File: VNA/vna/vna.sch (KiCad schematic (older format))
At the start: 4 parts, among them J1 USB_B_Micro, J2 Battery Cell Connection, J3 Pt1, J4 Pt2

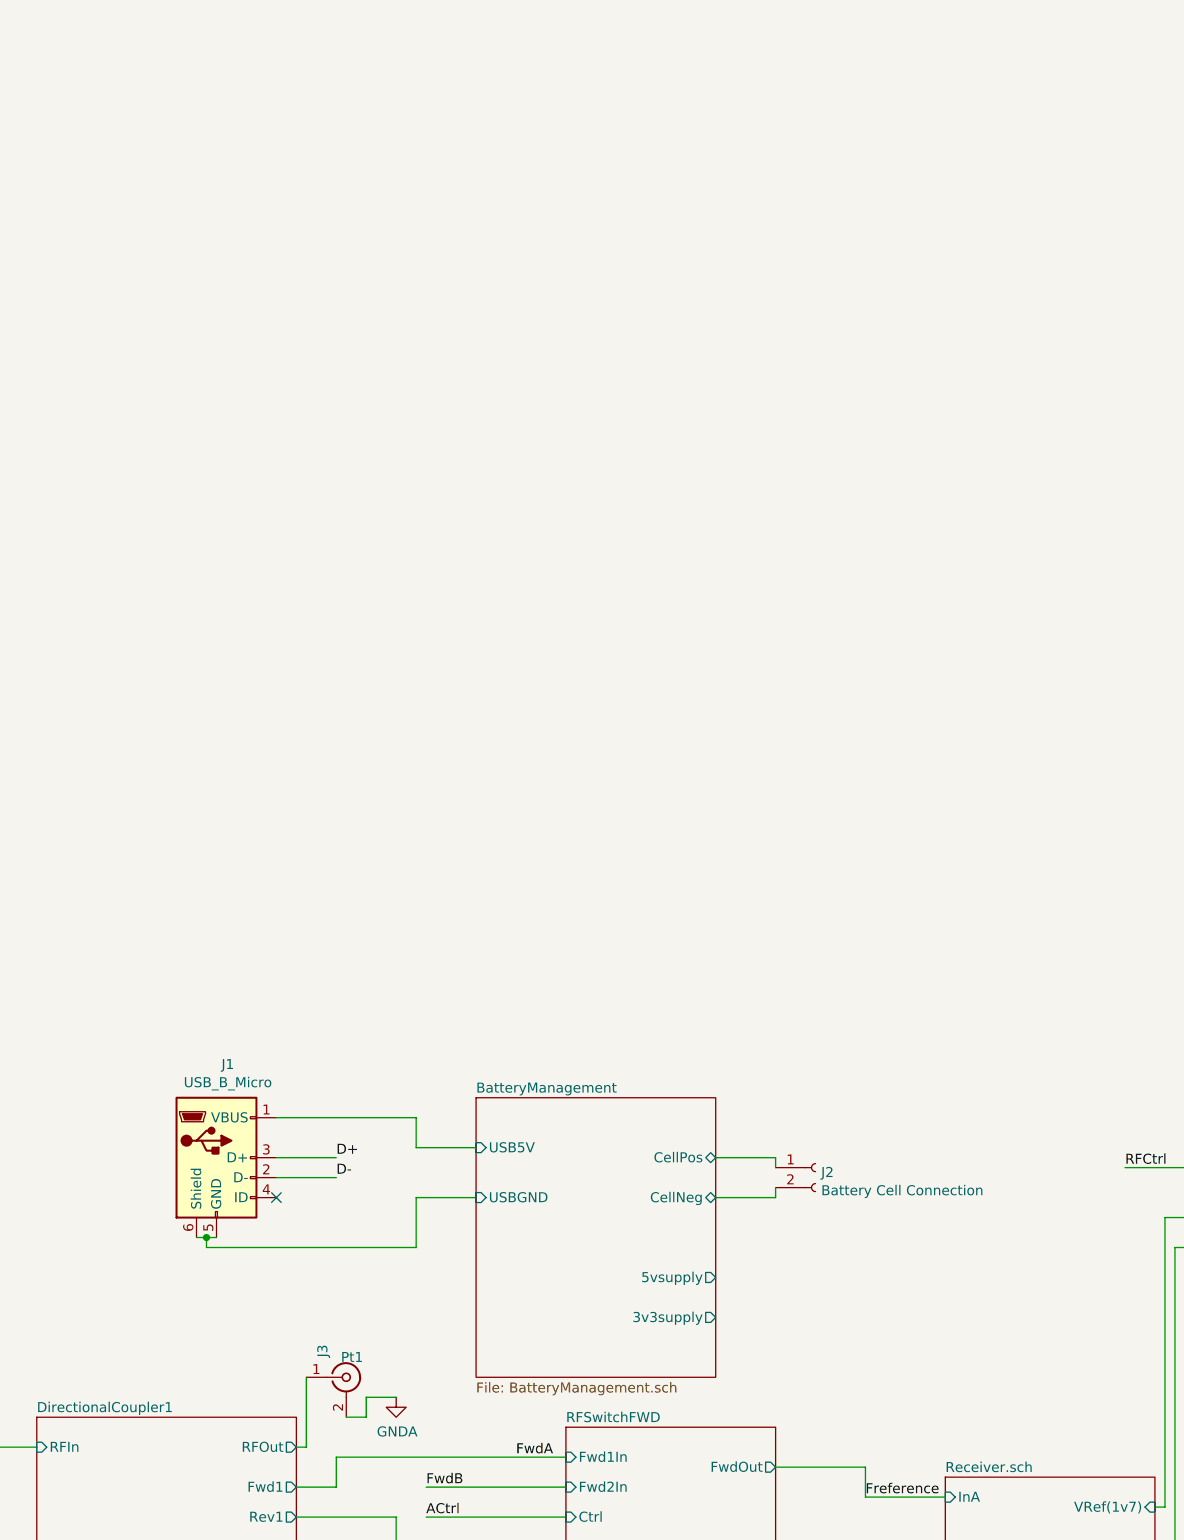
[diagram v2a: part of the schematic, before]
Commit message: changed inductors to a single transformer component
inductors in the directional couplers was changed to a single transformer

this will help with later layout opperations
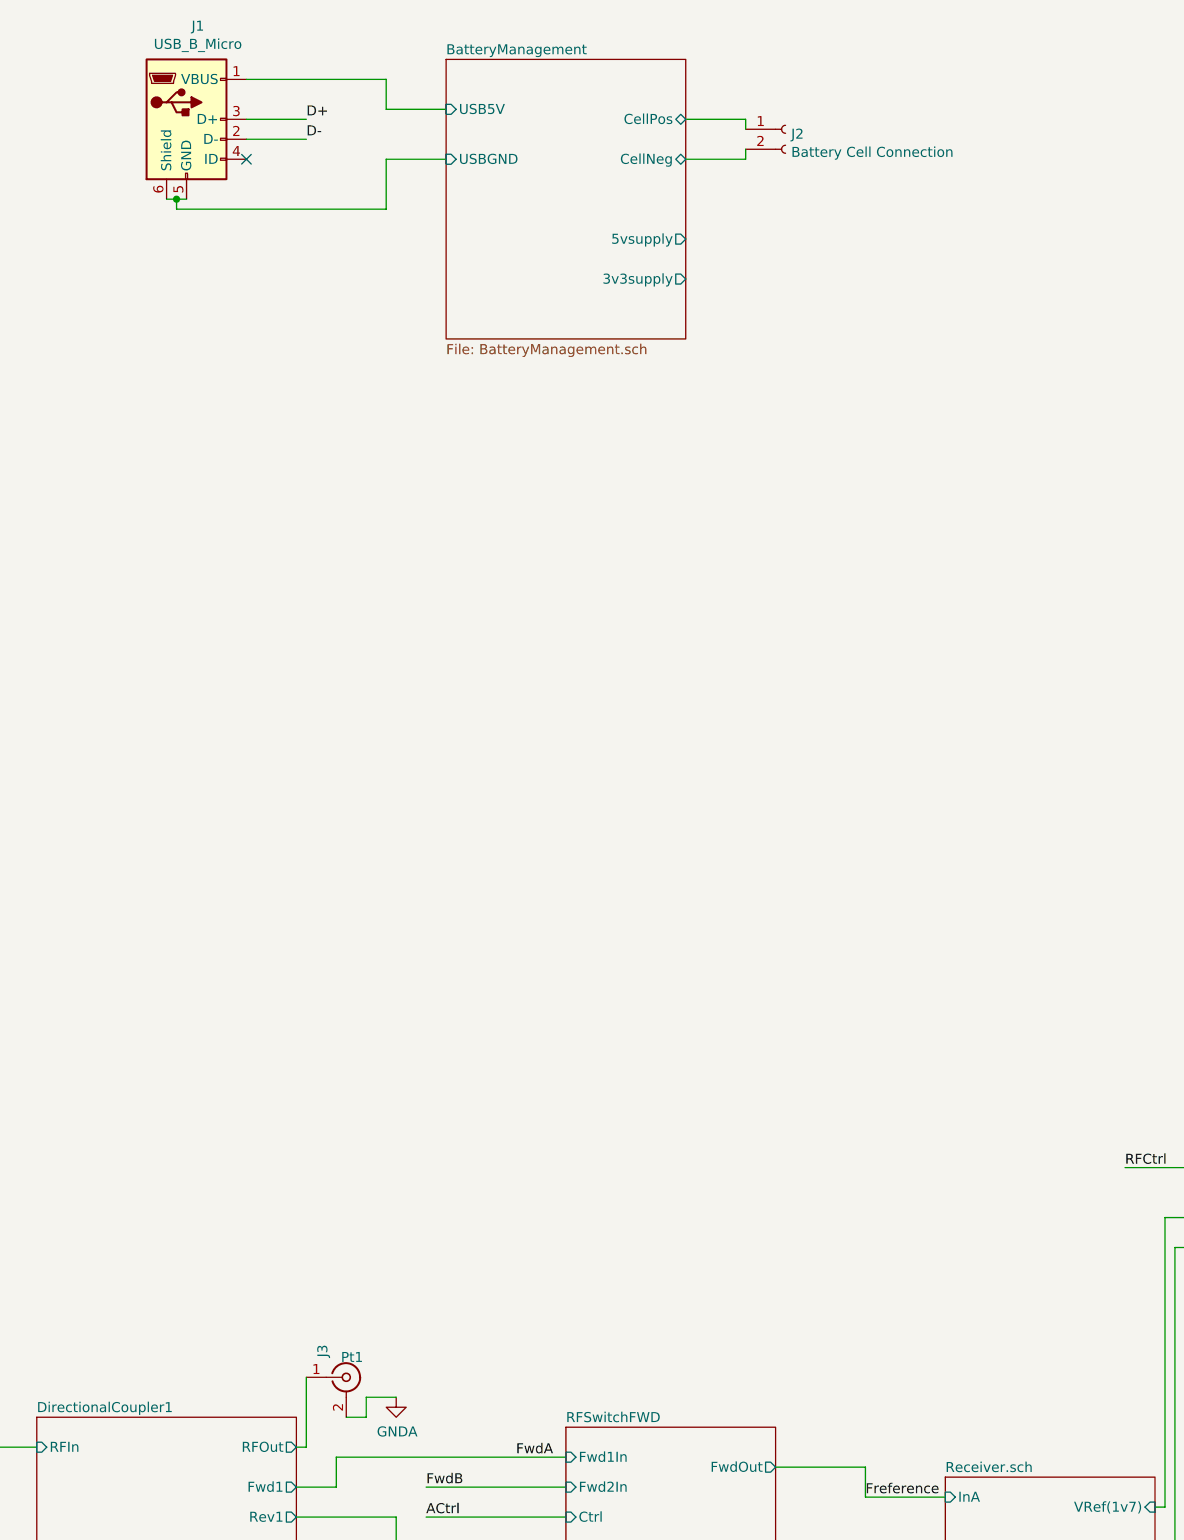
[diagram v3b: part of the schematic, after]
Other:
- moved on the sheet: J1, J2
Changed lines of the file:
@@
 BCtrl
 $Sheet
-S 5500 2250 1200 1400
+S 5350 -2950 1200 1400
 U 5CDF1C56
 F0 "BatteryManagement" 50
 F1 "BatteryManagement.sch" 50
-F2 "USB5V" I L 5500 2500 50
-F3 "USBGND" I L 5500 2750 50
-F4 "3v3supply" O R 6700 3350 50
-F5 "5vsupply" O R 6700 3150 50
-F6 "CellPos" B R 6700 2550 50
-F7 "CellNeg" B R 6700 2750 50
+F2 "USB5V" I L 5350 -2700 50
+F3 "USBGND" I L 5350 -2450 50
+F4 "3v3supply" O R 6550 -1850 50
+F5 "5vsupply" O R 6550 -2050 50
+F6 "CellPos" B R 6550 -2650 50
+F7 "CellNeg" B R 6550 -2450 50
 $EndSheet
 $Comp
 L Connector:USB_B_Micro J1
 U 1 1 5CE2753D
-P 4200 2550
-F 0 "J1" H 4257 3017 50  0000 C CNN
-F 1 "USB_B_Micro" H 4257 2926 50  0000 C CNN
-F 2 "" H 4350 2500 50  0001 C CNN
-F 3 "~" H 4350 2500 50  0001 C CNN
-	1    4200 2550
+P 4050 -2650
+F 0 "J1" H 4107 -2183 50  0000 C CNN
+F 1 "USB_B_Micro" H 4107 -2274 50  0000 C CNN
+F 2 "" H 4200 -2700 50  0001 C CNN
+F 3 "~" H 4200 -2700 50  0001 C CNN
+	1    4050 -2650
 	1    0    0    -1
 $EndComp
 Wire Wire Line
-	4500 2350 5200 2350
+	4350 -2850 5050 -2850
 Wire Wire Line
-	5200 2350 5200 2500
+	5050 -2850 5050 -2700
 Wire Wire Line
-	5200 2500 5500 2500
+	5050 -2700 5350 -2700
 Wire Wire Line
-	4100 2950 4150 2950
+	3950 -2250 4000 -2250
 Wire Wire Line
-	4150 2950 4150 3000
+	4000 -2250 4000 -2200
 Wire Wire Line
-	4150 3000 5200 3000
+	4000 -2200 5050 -2200
 Wire Wire Line
-	5200 3000 5200 2750
+	5050 -2200 5050 -2450
 Wire Wire Line
-	5200 2750 5500 2750
-Connection ~ 4150 2950
+	5050 -2450 5350 -2450
+Connection ~ 4000 -2250
 Wire Wire Line
-	4150 2950 4200 2950
+	4000 -2250 4050 -2250
 $Sheet
 S 9250 2300 900  950
@@
 Text Label 10700 2700 0    50   ~ 0
 D+
-NoConn ~ 4500 2750
+NoConn ~ 4350 -2450
 Wire Wire Line
-	4500 2550 4800 2550
+	4350 -2650 4650 -2650
 Wire Wire Line
-	4500 2650 4800 2650
-Text Label 4800 2550 0    50   ~ 0
+	4350 -2550 4650 -2550
+Text Label 4650 -2650 0    50   ~ 0
 D+
-Text Label 4800 2650 0    50   ~ 0
+Text Label 4650 -2550 0    50   ~ 0
 D-
 Wire Wire Line
@@
 L Connector:Conn_01x02_Female J2
 U 1 1 5CE4F062
-P 7200 2600
-F 0 "J2" H 7228 2576 50  0000 L CNN
-F 1 "Battery Cell Connection" H 7228 2485 50  0000 L CNN
-F 2 "" H 7200 2600 50  0001 C CNN
-F 3 "~" H 7200 2600 50  0001 C CNN
-	1    7200 2600
+P 7050 -2600
+F 0 "J2" H 7078 -2624 50  0000 L CNN
+F 1 "Battery Cell Connection" H 7078 -2715 50  0000 L CNN
+F 2 "" H 7050 -2600 50  0001 C CNN
+F 3 "~" H 7050 -2600 50  0001 C CNN
+	1    7050 -2600
 	1    0    0    -1
 $EndComp
 Wire Wire Line
-	6700 2550 7000 2550
+	6550 -2650 6850 -2650
 Wire Wire Line
-	7000 2550 7000 2600
+	6850 -2650 6850 -2600
 Wire Wire Line
-	6700 2750 7000 2750
+	6550 -2450 6850 -2450
 Wire Wire Line
-	7000 2750 7000 2700
+	6850 -2450 6850 -2500
 Wire Wire Line
 	1450 4350 1200 4350

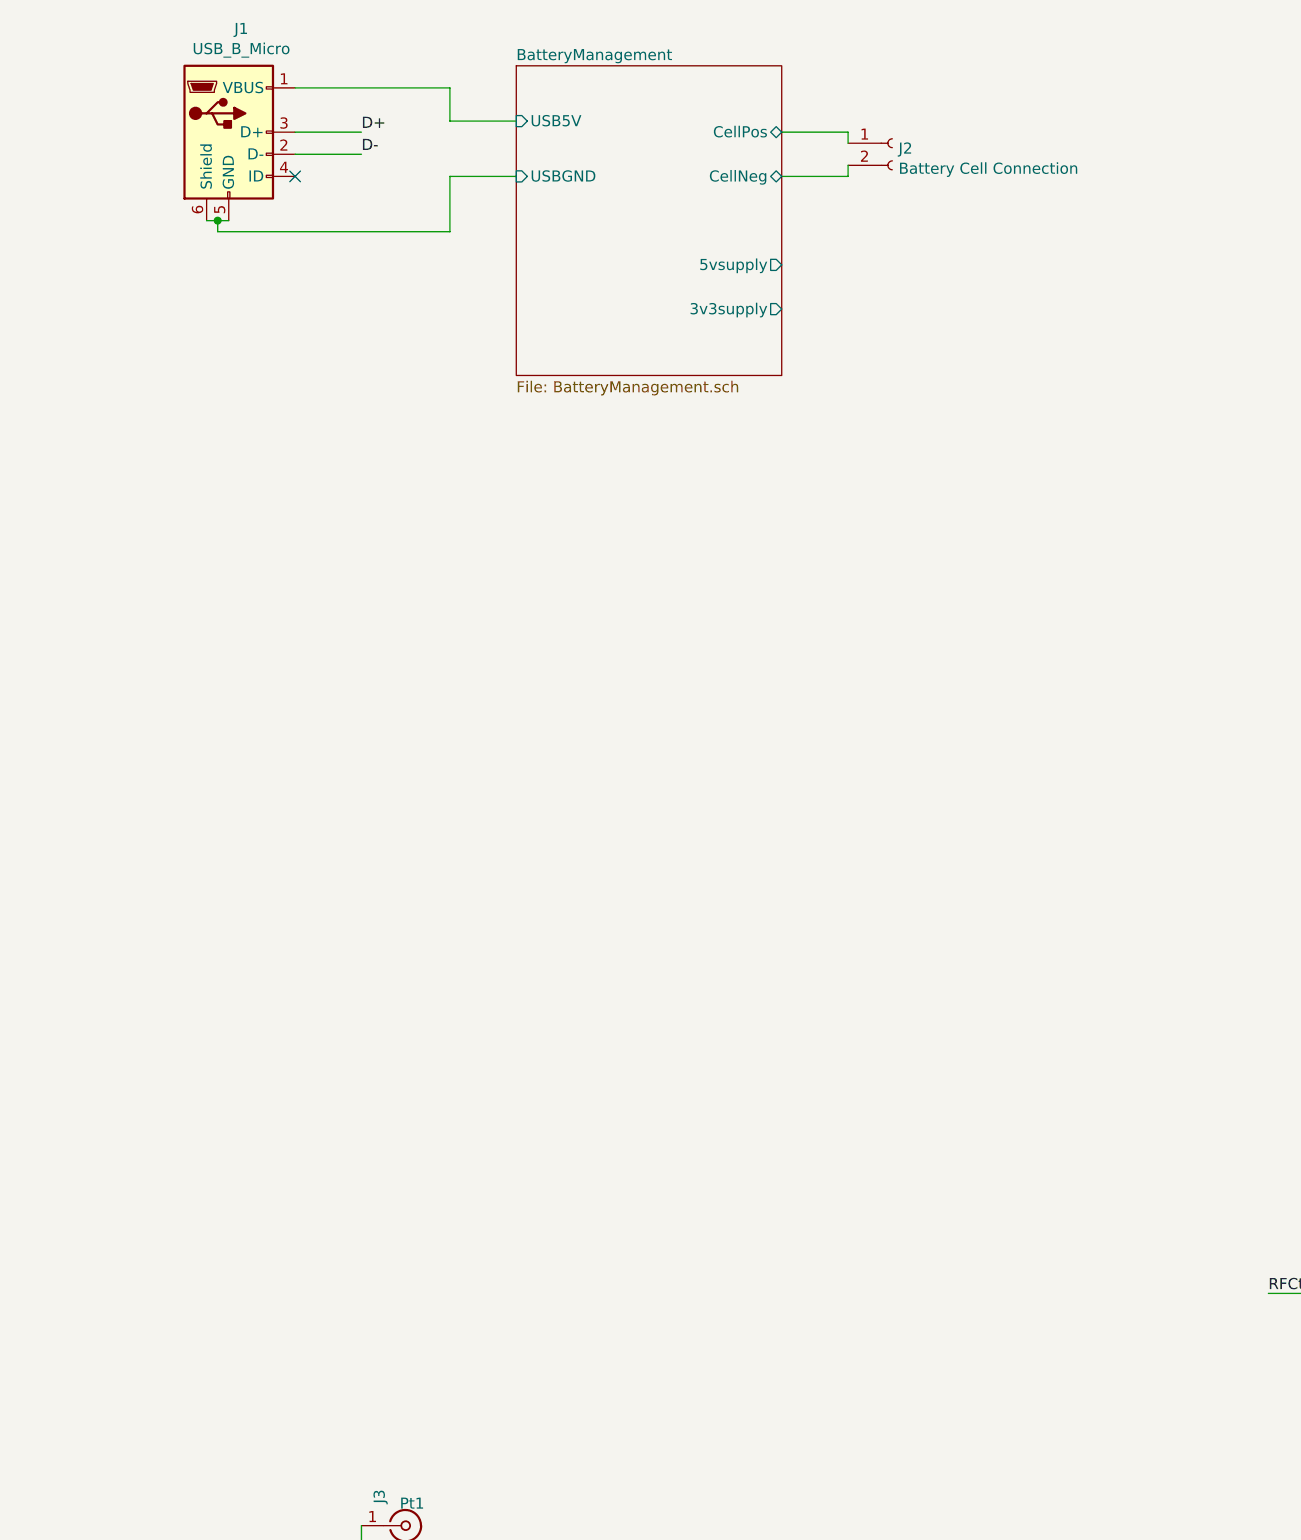
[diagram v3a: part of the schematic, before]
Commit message: micro-controller pins labelled
micro controller pins have been labelled, the pins on the bottom are yet to be linked to them.

still to wire up ftdi chip,

still to decide upon rf switch control schema.
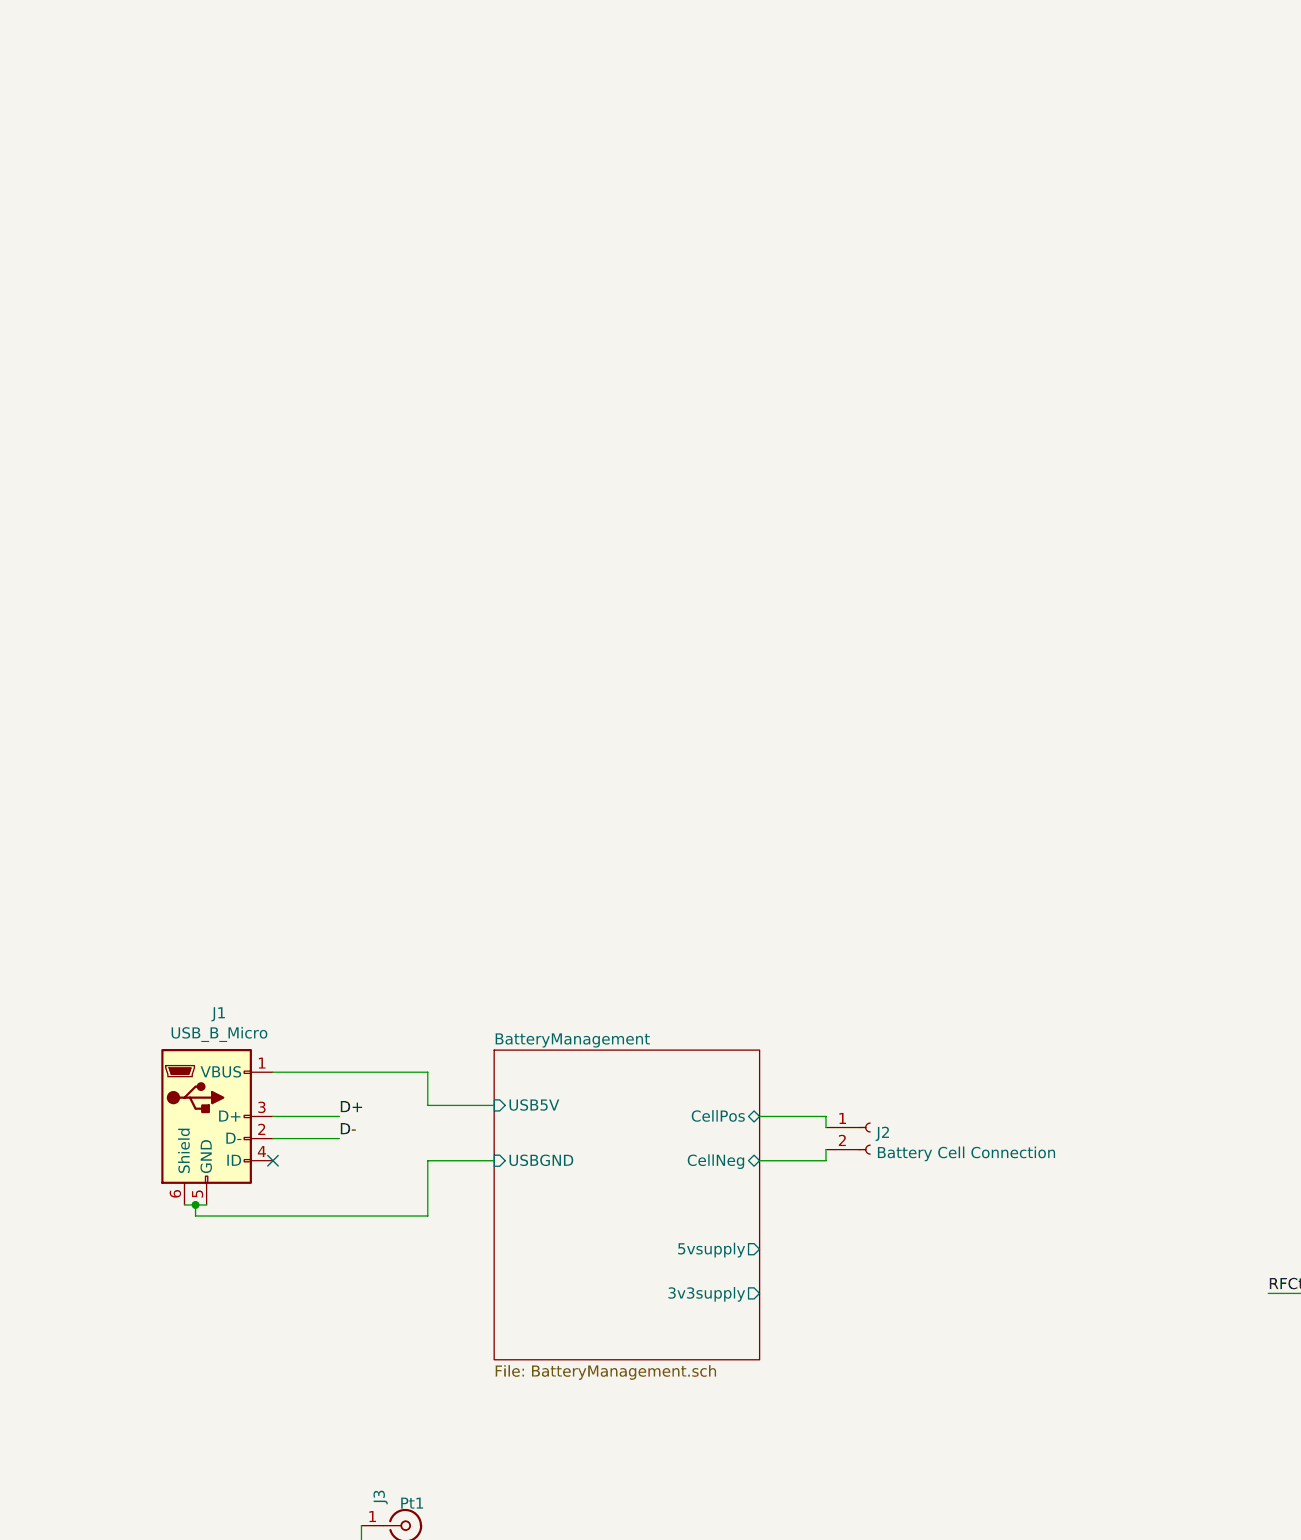
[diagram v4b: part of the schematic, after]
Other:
- moved on the sheet: J1, J2
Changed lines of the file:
@@
 BCtrl
 $Sheet
-S 5350 -2950 1200 1400
+S 5250 1500 1200 1400
 U 5CDF1C56
 F0 "BatteryManagement" 50
 F1 "BatteryManagement.sch" 50
-F2 "USB5V" I L 5350 -2700 50
-F3 "USBGND" I L 5350 -2450 50
-F4 "3v3supply" O R 6550 -1850 50
-F5 "5vsupply" O R 6550 -2050 50
-F6 "CellPos" B R 6550 -2650 50
-F7 "CellNeg" B R 6550 -2450 50
+F2 "USB5V" I L 5250 1750 50
+F3 "USBGND" I L 5250 2000 50
+F4 "3v3supply" O R 6450 2600 50
+F5 "5vsupply" O R 6450 2400 50
+F6 "CellPos" B R 6450 1800 50
+F7 "CellNeg" B R 6450 2000 50
 $EndSheet
 $Comp
 L Connector:USB_B_Micro J1
 U 1 1 5CE2753D
-P 4050 -2650
-F 0 "J1" H 4107 -2183 50  0000 C CNN
-F 1 "USB_B_Micro" H 4107 -2274 50  0000 C CNN
-F 2 "" H 4200 -2700 50  0001 C CNN
-F 3 "~" H 4200 -2700 50  0001 C CNN
-	1    4050 -2650
+P 3950 1800
+F 0 "J1" H 4007 2267 50  0000 C CNN
+F 1 "USB_B_Micro" H 4007 2176 50  0000 C CNN
+F 2 "" H 4100 1750 50  0001 C CNN
+F 3 "~" H 4100 1750 50  0001 C CNN
+	1    3950 1800
 	1    0    0    -1
 $EndComp
 Wire Wire Line
-	4350 -2850 5050 -2850
+	4250 1600 4950 1600
 Wire Wire Line
-	5050 -2850 5050 -2700
+	4950 1600 4950 1750
 Wire Wire Line
-	5050 -2700 5350 -2700
+	4950 1750 5250 1750
 Wire Wire Line
-	3950 -2250 4000 -2250
+	3850 2200 3900 2200
 Wire Wire Line
-	4000 -2250 4000 -2200
+	3900 2200 3900 2250
 Wire Wire Line
-	4000 -2200 5050 -2200
+	3900 2250 4950 2250
 Wire Wire Line
-	5050 -2200 5050 -2450
+	4950 2250 4950 2000
 Wire Wire Line
-	5050 -2450 5350 -2450
-Connection ~ 4000 -2250
+	4950 2000 5250 2000
+Connection ~ 3900 2200
 Wire Wire Line
-	4000 -2250 4050 -2250
+	3900 2200 3950 2200
 $Sheet
 S 9250 2300 900  950
@@
 Text Label 10700 2700 0    50   ~ 0
 D+
-NoConn ~ 4350 -2450
+NoConn ~ 4250 2000
 Wire Wire Line
-	4350 -2650 4650 -2650
+	4250 1800 4550 1800
 Wire Wire Line
-	4350 -2550 4650 -2550
-Text Label 4650 -2650 0    50   ~ 0
+	4250 1900 4550 1900
+Text Label 4550 1800 0    50   ~ 0
 D+
-Text Label 4650 -2550 0    50   ~ 0
+Text Label 4550 1900 0    50   ~ 0
 D-
 Wire Wire Line
@@
 L Connector:Conn_01x02_Female J2
 U 1 1 5CE4F062
-P 7050 -2600
-F 0 "J2" H 7078 -2624 50  0000 L CNN
-F 1 "Battery Cell Connection" H 7078 -2715 50  0000 L CNN
-F 2 "" H 7050 -2600 50  0001 C CNN
-F 3 "~" H 7050 -2600 50  0001 C CNN
-	1    7050 -2600
+P 6950 1850
+F 0 "J2" H 6978 1826 50  0000 L CNN
+F 1 "Battery Cell Connection" H 6978 1735 50  0000 L CNN
+F 2 "" H 6950 1850 50  0001 C CNN
+F 3 "~" H 6950 1850 50  0001 C CNN
+	1    6950 1850
 	1    0    0    -1
 $EndComp
 Wire Wire Line
-	6550 -2650 6850 -2650
+	6450 1800 6750 1800
 Wire Wire Line
-	6850 -2650 6850 -2600
+	6750 1800 6750 1850
 Wire Wire Line
-	6550 -2450 6850 -2450
+	6450 2000 6750 2000
 Wire Wire Line
-	6850 -2450 6850 -2500
+	6750 2000 6750 1950
 Wire Wire Line
 	1450 4350 1200 4350
